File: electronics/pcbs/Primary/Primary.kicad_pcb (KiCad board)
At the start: 2 copper layers, 102 x 53.3 mm, 27 parts, among them J1 Line Sensor 1, J10 I2C Bus, J11 I2C Bus, J12 Battery, J13 Pololu_D24V50F5, J14 Magnet, J2 Line Sensor 2, J3 Line Sensor 3, J4 Line Sensor 4, J5 Line Sensor 5, J6 Line Sensor 6, J7 Servo, J8 Pololu_DRV8834, J9 Stepper Motor, P1 Digital, P10 CONN_01X01, P11 CONN_01X01, P12 CONN_01X01, P13 CONN_01X01, P2 Power, P3 Analog, P4 Analog, P5 PWM, P6 PWM, P7 Communication, P8 CONN_01X01, P9 CONN_01X01

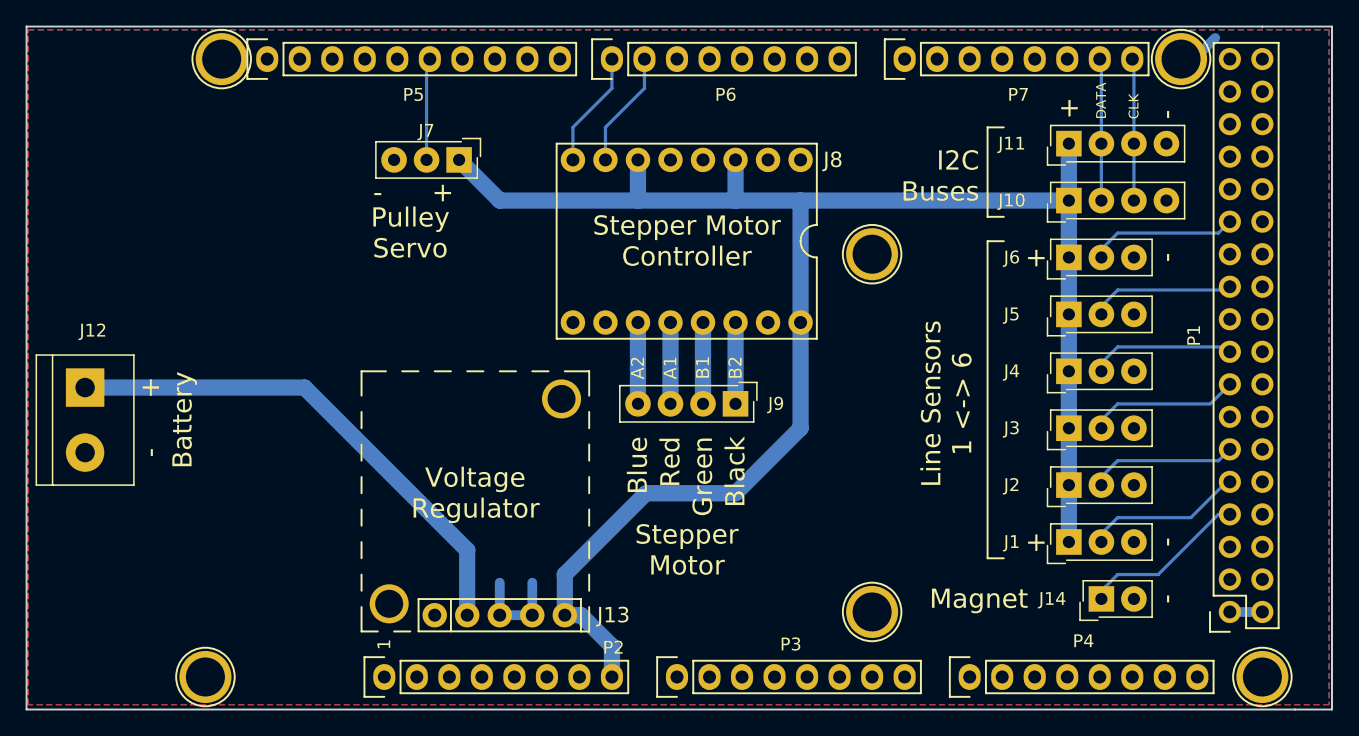
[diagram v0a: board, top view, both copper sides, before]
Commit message: Primary PCB: Removed one of the I2C bus sockets - we'll only need one.
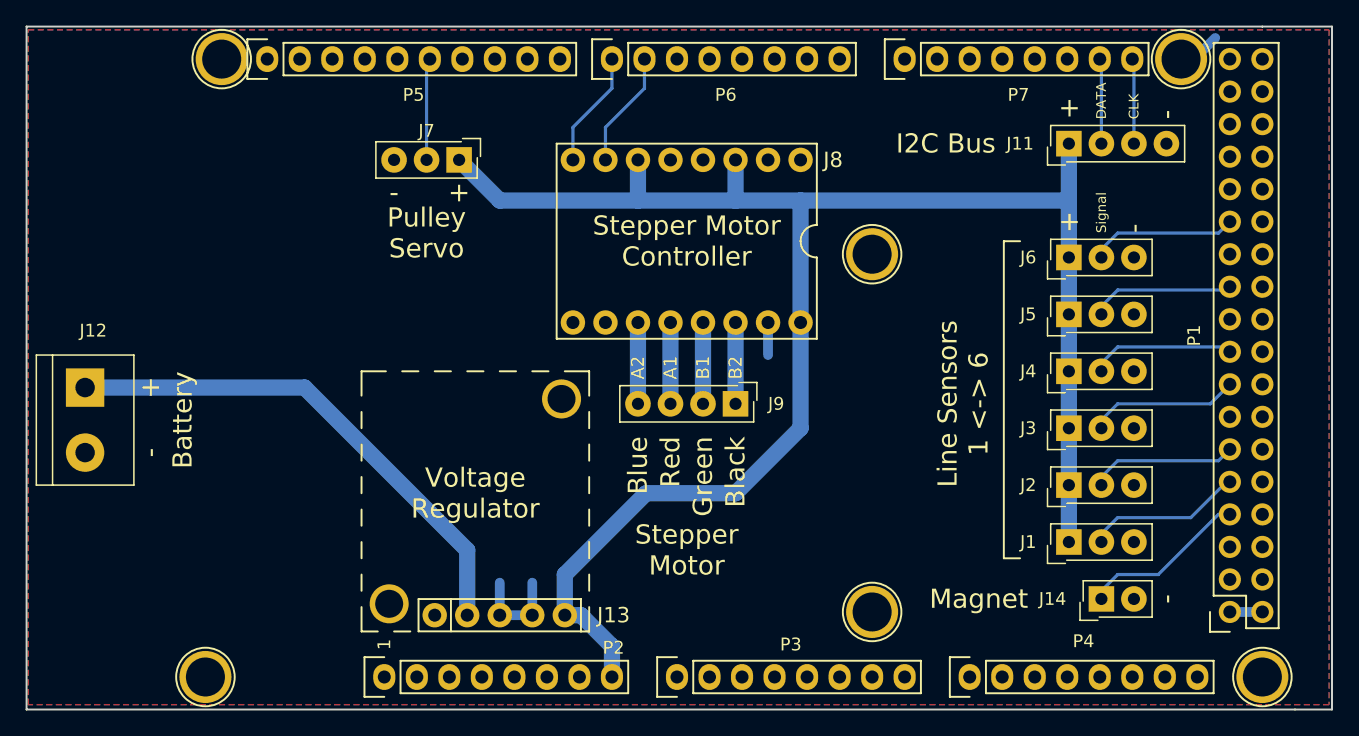
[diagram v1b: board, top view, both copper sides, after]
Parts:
- removed J10: I2C Bus, Connectors_Samtec:SL-104-X-XX_1x04
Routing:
- net /20(SDA): track 11.1 -> 6.66 mm
- net /21(SCL): track 11.1 -> 6.66 mm
- net GND: track 13.5 -> 16.1 mm
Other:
- board text added: "I2C Bus"
- board text added: "Signal"
- board text removed: "I2C Buses"

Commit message: Primary PCB: Added pinout labels and pin labels to silkscreen.
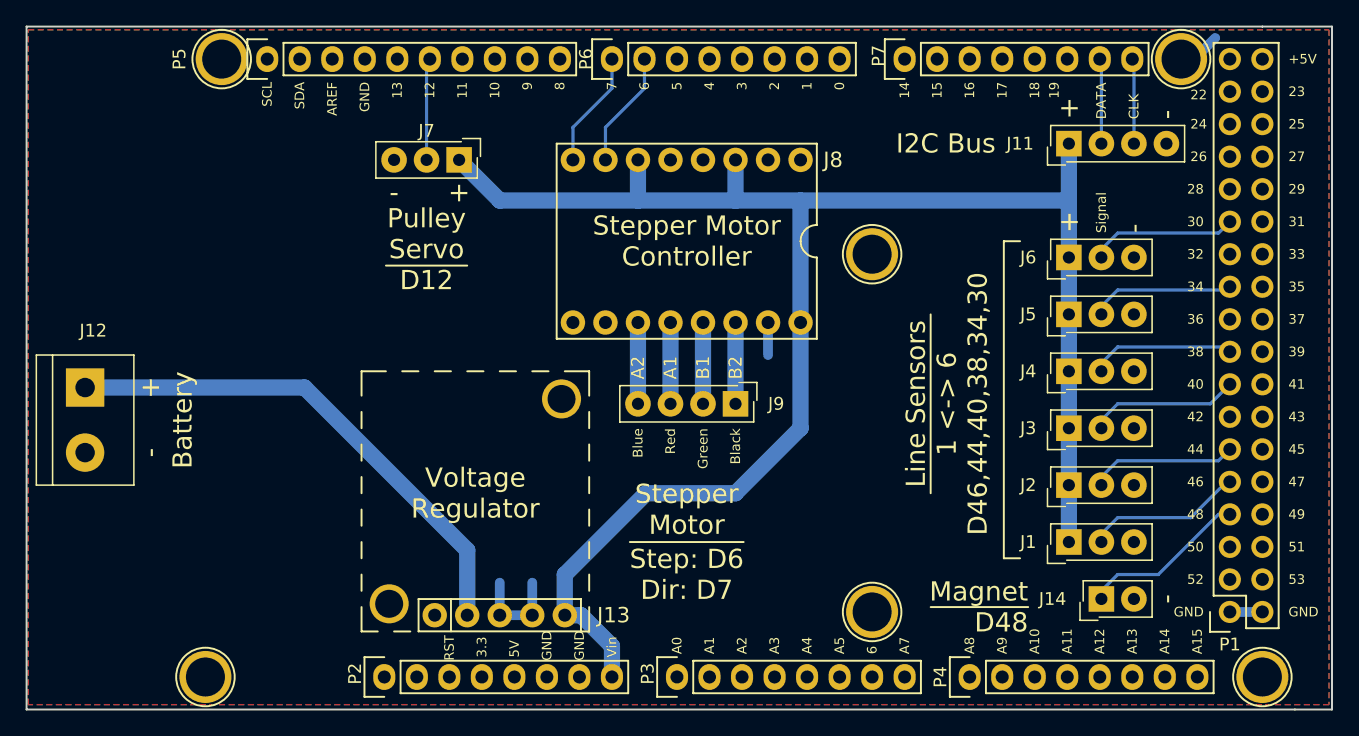
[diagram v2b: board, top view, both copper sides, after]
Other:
- board text added: "+5V"
- board text added: "0"
- board text added: "10"
- board text added: "11"
- board text added: "12"
- board text added: "13"
- board text added: "14"
- board text added: "15"
- board text added: "16"
- board text added: "17"
- board text added: "18"
- board text added: "19"
- board text added: "2"
- board text added: "22"
- board text added: "23"
- board text added: "24"
- board text added: "25"
- board text added: "26"
- board text added: "27"
- board text added: "28"
- board text added: "29"
- board text added: "3"
- board text added: "3.3"
- board text added: "30"
- board text added: "31"
- board text added: "32"
- board text added: "33"
- board text added: "34"
- board text added: "35"
- board text added: "36"
- board text added: "37"
- board text added: "38"
- board text added: "39"
- board text added: "4"
- board text added: "40"
- board text added: "41"
- board text added: "42"
- board text added: "43"
- board text added: "44"
- board text added: "45"
- board text added: "46"
- board text added: "47"
- board text added: "48"
- board text added: "49"
- board text added: "5"
- board text added: "50"
- board text added: "51"
- board text added: "52"
- board text added: "53"
- board text added: "5V"
- board text added: "6"
- board text added: "7"
- board text added: "8"
- board text added: "9"
- board text added: "A0"
- board text added: "A10"
- board text added: "A11"
- board text added: "A12"
- board text added: "A13"
- board text added: "A14"
- board text added: "A15"
- board text added: "A3"
- board text added: "A4"
- board text added: "A5"
- board text added: "A7"
- board text added: "A8"
- board text added: "A9"
- board text added: "AREF"
- board text added: "GND"
- board text added: "Line Sensors 1 <-> 6 D46,44,40,38,34,30"
- board text added: "Magnet D48"
- board text added: "Pulley Servo D12"
- board text added: "RST"
- board text added: "SCL"
- board text added: "SDA"
- board text added: "Step: D6 Dir: D7"
- board text added: "Vin"
- board text removed: "Line Sensors 1 <-> 6"
- board text removed: "Magnet"
- board text removed: "Pulley Servo"
